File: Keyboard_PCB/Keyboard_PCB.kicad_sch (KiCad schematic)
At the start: 32 parts, among them J2 JTAG, U1 STM32H7B0VBTx, Y1 25MHz, Y2 32.768 KHz

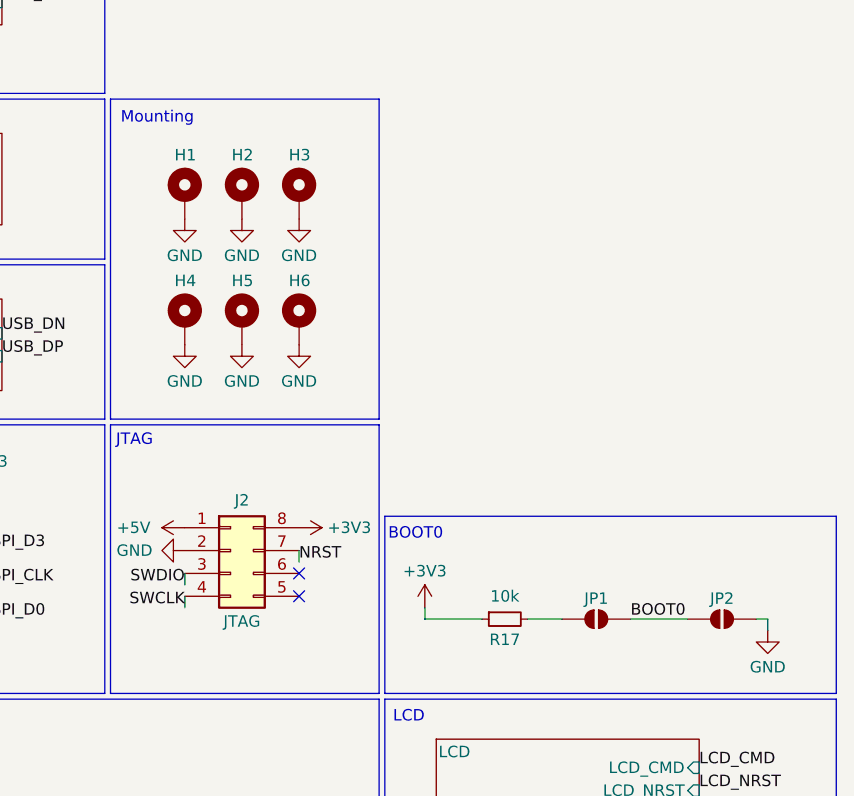
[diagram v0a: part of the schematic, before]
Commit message: Fixed errors in BOM file
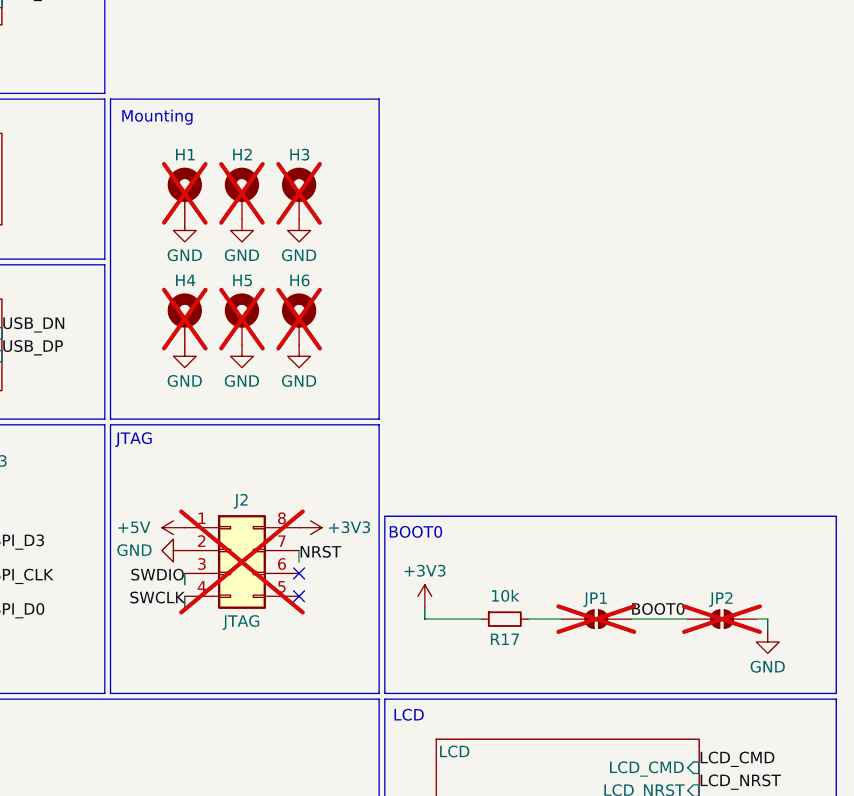
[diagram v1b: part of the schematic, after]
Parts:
- C10, C11, C12, C13: LCSC C52923 -> C1547
- H1, H2, H3, H4, H5, H6, J2, JP1, JP2: now not fitted
- U1: LCSC (none) -> C730227
- U4: LCSC (none) -> C5267629
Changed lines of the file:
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@@
 		(in_bom no)
 		(on_board yes)
-		(dnp no)
+		(dnp yes)
 		(property "Reference" "JP1"
 			(at 214.63 124.714 0)
@@
 		(in_bom no)
 		(on_board yes)
-		(dnp no)
+		(dnp yes)
 		(property "Reference" "H6"
 			(at 182.88 89.408 0)
@@
 			)
 		)
+		(property "LCSC" "C730227"
+			(at 60.96 101.6 0)
+			(effects
+				(font
+					(size 1.27 1.27)
+				)
+				(hide yes)
+			)
+		)
 		(pin "17"
 		)
@@
 		(in_bom no)
 		(on_board yes)
-		(dnp no)
+		(dnp yes)
 		(property "Reference" "H3"
 			(at 182.88 75.438 0)
@@
 		(in_bom no)
 		(on_board yes)
-		(dnp no)
+		(dnp yes)
 		(property "Reference" "H2"
 			(at 176.53 75.438 0)
@@
 			)
 		)
+		(property "LCSC" " C5267629"
+			(at 134.62 110.49 0)
+			(effects
+				(font
+					(size 1.27 1.27)
+				)
+				(hide yes)
+			)
+		)
 		(pin "2"
 		)
@@
 			)
 		)
-		(property "LCSC" "C52923"
+		(property "LCSC" "C1547"
 			(at 137.16 186.69 0)
 			(effects
@@
 			)
 		)
-		(property "LCSC" "C52923"
+		(property "LCSC" "C1547"
 			(at 153.67 186.69 0)
 			(effects
@@
 		(in_bom no)
 		(on_board yes)
-		(dnp no)
+		(dnp yes)
 		(property "Reference" "H4"
 			(at 170.18 89.408 0)
@@
 		(in_bom no)
 		(on_board yes)
-		(dnp no)
+		(dnp yes)
 		(property "Reference" "H5"
 			(at 176.53 89.408 0)
@@
 			)
 		)
-		(property "LCSC" "C52923"
+		(property "LCSC" "C1547"
 			(at 166.37 186.69 0)
 			(effects
@@
 		(in_bom yes)
 		(on_board yes)
-		(dnp no)
+		(dnp yes)
 		(property "Reference" "J2"
 			(at 175.26 113.792 0)
@@
 		(in_bom no)
 		(on_board yes)
-		(dnp no)
+		(dnp yes)
 		(property "Reference" "JP2"
 			(at 228.6 124.714 0)
@@
 			)
 		)
-		(property "LCSC" "C52923"
+		(property "LCSC" "C1547"
 			(at 124.46 186.69 0)
 			(effects
@@
 		(in_bom no)
 		(on_board yes)
-		(dnp no)
+		(dnp yes)
 		(property "Reference" "H1"
 			(at 170.18 75.438 0)

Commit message: Layout progress
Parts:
- removed C8, C9: 100n, Capacitor_SMD:C_0402_1005Metric, symbol Device:C_Small
- removed J2: JTAG, Connector_PinHeader_2.00mm:PinHeader_2x04_P2.00mm_Vertical, symbol Connector_Generic:Conn_02x04_Counter_Clockwise
- removed JP1, JP2: SolderJumper_2_Open, Jumper:SolderJumper-2_P1.3mm_Open_TrianglePad1.0x1.5mm, symbol Jumper:SolderJumper_2_Open
- removed R17: 10k, Resistor_SMD:R_0603_1608Metric, symbol Device:R_Small
- added C15, C16: 1u, Capacitor_SMD:C_0402_1005Metric, symbol Device:C_Small
- added C27, C28: 100n, Capacitor_SMD:C_0402_1005Metric, symbol Device:C_Small
- added D69: BAT54C, Package_TO_SOT_SMD:SOT-23, symbol Diode:BAT54C
- added D70: PWR, LED_SMD:LED_0603_1608Metric, symbol Device:LED
- added D71: STATUS, LED_SMD:LED_0603_1608Metric, symbol Device:LED
- added J3: JTAG, Connector_PinHeader_2.00mm:PinHeader_1x04_P2.00mm_Vertical, symbol Connector_Generic:Conn_01x04
- added R18: 5k1, Resistor_SMD:R_0402_1005Metric, symbol Device:R_Small
- added R19: 1k, Resistor_SMD:R_0402_1005Metric, symbol Device:R_Small
- added R20, R21: 10k, Resistor_SMD:R_0402_1005Metric, symbol Device:R_Small
- added SW71, SW72: BTN, Button_Switch_SMD:SW_SPST_TL3342, symbol Switch:SW_Push
- added TP1, TP2, TP3, TP4, TP5, TP6: TestPoint, TestPoint:TestPoint_THTPad_D2.0mm_Drill1.0mm, symbol Connector:TestPoint
- added U3: ~, Custom:SOT-25, symbol Marijn:AP7343
- C1: value 1u -> 100n; LCSC C52923 -> (none)
- C2: value 10n -> 100n; LCSC C15195 -> (none)
- C3: value 4u7 -> 100n; LCSC C23733 -> (none)
- C4, C5, C7: LCSC C1525 -> (none)
- C6: value 100n -> 4.7u; LCSC C1525 -> (none)
- L1: footprint Inductor_SMD:L_0603_1608Metric -> Inductor_SMD:L_0805_2012Metric; LCSC C1035 -> C139245
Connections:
- net +3.3VA: now also C7.1, L1.2; no longer C1.1, C2.1, L1.1
- net +3V3: now also C1.1, C2.1, L1.1, C16.1, D69.2, J3.1 (Pin_1), R18.1, R19.1, R20.1, SW71.2, U3.5 (VOUT); no longer C7.1, L1.2
- net +5V: now also C15.1, U3.1 (VIN), U3.3 (EN)
- net BOOT0: now also R21.1, SW71.1
- net GND: now also C15.2, C16.2, C27.1, C28.1, D70.1 (K), J3.4 (Pin_4), R21.2, SW72.2, U3.2 (GND)
- net NRST: now also C28.2, R20.2, SW72.1
- net QSPI_CLK: now also TP5.1
- net QSPI_D0: now also TP6.1
- net QSPI_D1: now also TP2.1
- net QSPI_D2: now also TP3.1
- net QSPI_D3: now also TP4.1
- net QSPI_NCS: now also TP1.1
- net SWCLK: now also J3.3 (Pin_3)
- net SWDIO: now also J3.2 (Pin_2)
- net ROT1_SW: now reaches U1.89 (PB3)
- net TIM3_CH1: now reaches U1.90 (PB4)
- net TIM3_CH2: now reaches U1.91 (PB5)
- net ROT_SW renamed ROT0_SW
- net TIM_CH1 renamed TIM2_CH1
- net TIM_CH2 renamed TIM2_CH2
- new net: D70.2 (A), R18.2
- new net: D71.2 (A), R19.2
- new net STATUS: D71.1 (K)
- new net VBAT: C27.2, D69.3
- new net VB_IN: D69.1
- no-connect marks 42 -> 37
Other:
- removed sheet Power
- sheet Grid ports: added ROT0_A, ROT0_B, ROT0_SW, ROT1_A, ROT1_B, ROT1_SW; removed ROT_A, ROT_B, ROT_SW
- note added: "BOOT0 / NRST"
- note added: "Bypass / Filter"
- note added: "LED"
- note added: "TODO: battery header!!"
- note added: "VBAT"
- note removed: "BOOT0"
- note removed: "Bypass"
- note removed: "VDDA_Filter"
- moved on the sheet: H1, H2, H3, H4, H5, H6, U4

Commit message: Layout progress
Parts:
- added J2: Battery, Connector_PinHeader_2.00mm:PinHeader_2x01_P2.00mm_Vertical, symbol Connector_Generic:Conn_02x01
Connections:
- net +3V3: no longer U1.6 (VBAT)
- net GND: now also J2.1 (Pin_1)
- net VBAT: now also U1.6 (VBAT)
- net VB_IN: now also J2.2 (Pin_2)
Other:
- moved on the sheet: D70, D71, R18, R19

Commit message: Layout V1
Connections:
- net STATUS: now also U1.15 (PC0)
- no-connect marks 37 -> 36
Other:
- note added: "TODO: battery charging"
- note removed: "TODO: battery header!!"
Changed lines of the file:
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@@
-	)
-	(no_connect
-		(at 83.82 124.46)
 	)
 	(no_connect
@@
 		(pts
 			(xy 40.64 54.61) (xy 40.64 53.34)
+		)
+		(stroke
+			(width 0)
+			(type default)
+		)
+	)
+	(wire
+		(pts
+			(xy 83.82 125.73) (xy 83.82 124.46)
 		)
 		(stroke
@@
 		)
 	)
+	(text "TODO: battery charging"
+		(exclude_from_sim no)
+		(at 179.07 77.724 0)
+		(effects
+			(font
+				(size 1.27 1.27)
+			)
+		)
+	)
 	(text "USB"
 		(exclude_from_sim no)
@@
 		)
 	)
-	(text "TODO:\nbattery header!!"
-		(exclude_from_sim no)
-		(at 195.072 56.134 0)
-		(effects
-			(font
-				(size 1.27 1.27)
-			)
-		)
-	)
 	(text "LED"
 		(exclude_from_sim no)
@@
 		)
 	)
+	(label "STATUS"
+		(at 83.82 125.73 0)
+		(fields_autoplaced yes)
+		(effects
+			(font
+				(size 1.27 1.27)
+			)
+			(justify left bottom)
+		)
+	)

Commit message: Finished Layout V1
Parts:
- added J4: EBUS, Connector_PinHeader_2.00mm:PinHeader_2x04_P2.00mm_Vertical, symbol Connector_Generic:Conn_02x04_Counter_Clockwise
- added R17: 47, Resistor_SMD:R_0603_1608Metric, symbol Device:R_Small
- added R22: 2k2, Resistor_SMD:R_0603_1608Metric, symbol Device:R_Small
- C1, C10, C11, C12, C13, C15, C16, C2, C21, C22, C27, C28, C3, C4, C5, C7: footprint Capacitor_SMD:C_0402_1005Metric -> Capacitor_SMD:C_0603_1608Metric
- C6: value 4.7u -> 4u7; footprint Capacitor_SMD:C_0402_1005Metric -> Capacitor_SMD:C_0603_1608Metric
- H1, H2, H3, H4, H5, H6, TP1, TP2, TP3, TP4, TP5, TP6: now fitted
- R18, R19, R2, R20, R21, R3: footprint Resistor_SMD:R_0402_1005Metric -> Resistor_SMD:R_0603_1608Metric
- SW71, SW72: footprint Button_Switch_SMD:SW_SPST_TL3342 -> Button_Switch_SMD:SW_SPST_PTS810; LCSC C2886897 -> C2681476
- U3: value ~ -> AP7343
- U4: value ~ -> M95P32
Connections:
- net +3V3: now also R17.2, R22.2
- net GND: now also J4.8 (Pin_8)
- net EBUS_TX: now reaches U1.63 (PC6)
- net EBUS_TX: now also J4.2 (Pin_2)
- net SPI3_NCS: now reaches U1.66 (PC9)
- net SPI3_NCS: now also J4.3 (Pin_3)
- net EBUS_SENSE: now reaches U1.7 (PC13)
- net EBUS_SENSE: now also J4.7 (Pin_7), R22.1
- net SPI3_SCK: now reaches U1.78 (PC10)
- net SPI3_SCK: now also J4.4 (Pin_4)
- net SPI3_MISO: now reaches U1.79 (PC11)
- net SPI3_MISO: now also J4.6 (Pin_6)
- net SPI3_MOSI: now reaches U1.80 (PC12)
- net SPI3_MOSI: now also J4.5 (Pin_5)
- new net: J4.1 (Pin_1), R17.1
- no-connect marks 36 -> 30
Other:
- note added: "Expansion BUS: 1. connection detection pin 1p 2. power 2p 3. tx only uart for keypresses 1p 4. SPI bus 4p TODO: bus takes up almost whole width of pcb topside"

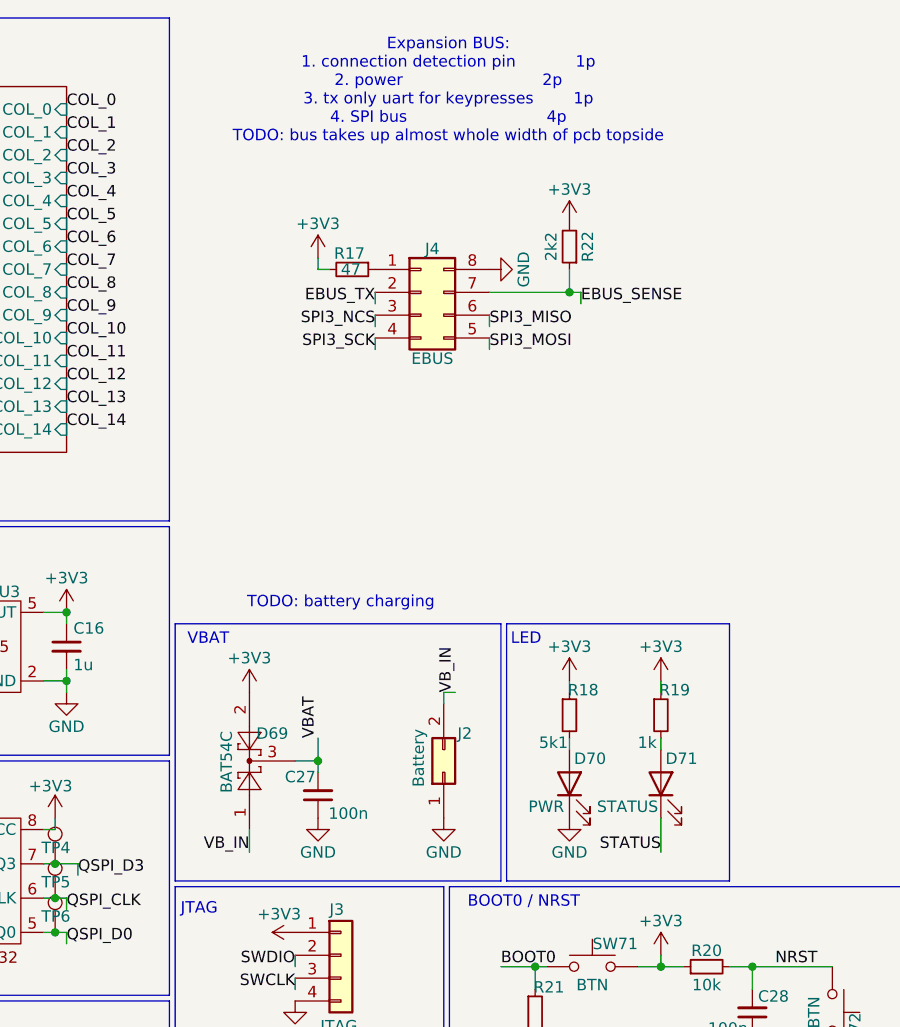
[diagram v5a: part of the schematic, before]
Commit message: Added battery charging support
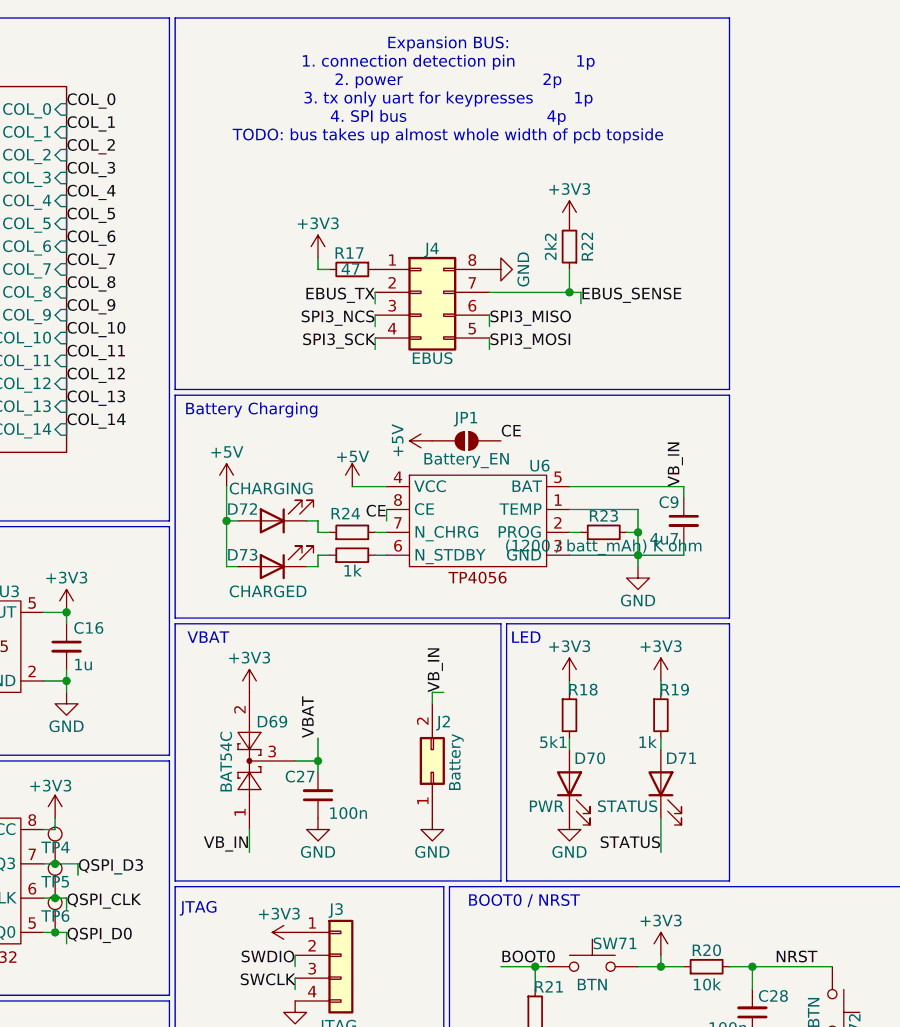
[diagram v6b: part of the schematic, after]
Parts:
- added C9: 4u7, Capacitor_SMD:C_0603_1608Metric, symbol Device:C_Small
- added D72: CHARGING, LED_SMD:LED_0603_1608Metric, symbol Device:LED
- added D73: CHARGED, LED_SMD:LED_0603_1608Metric, symbol Device:LED
- added JP1: Battery_EN, Jumper:SolderJumper-2_P1.3mm_Open_TrianglePad1.0x1.5mm, symbol Jumper:SolderJumper_2_Open
- added R23: (1200 / batt_mAh) K ohm, Resistor_SMD:R_0603_1608Metric, symbol Device:R_Small
- added R24, R25: 1k, Resistor_SMD:R_0603_1608Metric, symbol Device:R_Small
- added U6: ~, Package_SO:MSOP-8_3x3mm_P0.65mm, symbol Marijn:TP4056
- J2: footprint Connector_PinHeader_2.00mm:PinHeader_2x01_P2.00mm_Vertical -> Connector_PinHeader_2.00mm:PinHeader_1x02_P2.00mm_Vertical
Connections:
- net +5V: now also D72.2 (A), D73.2 (A), JP1.1 (A), U6.4 (VCC)
- net GND: now also C9.2, R23.2, U6.1 (TEMP), U6.3 (GND)
- net VB_IN: now also C9.1, U6.5 (BAT)
- new net: R23.1, U6.2 (PROG)
- new net: R25.2, U6.6 (N_STDBY)
- new net: R24.2, U6.7 (N_CHRG)
- new net: D72.1 (K), R24.1
- new net: D73.1 (K), R25.1
- new net CE: JP1.2 (B), U6.8 (CE)
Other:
- note added: "Battery Charging"
- note removed: "TODO: battery charging"
